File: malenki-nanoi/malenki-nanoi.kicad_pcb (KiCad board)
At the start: 4 copper layers, 19 x 32 mm, 45 parts, among them J1 Conn_01x02_Male-Connector, J2 Conn_01x08_Male, J3 Conn_01x02, J4 Conn_01x02_Male-Connector, J5 Conn_01x02_Male-Connector, J6 Conn_01x02_Male-Connector, U1 A7105, U2 AIC1734-33GUTR, U3 ATtiny1616-M, U4 DRV8837DSGR, U5 DRV8837DSGR, U6 DRV8837DSGR, Y1 16 Mhz 20ppm

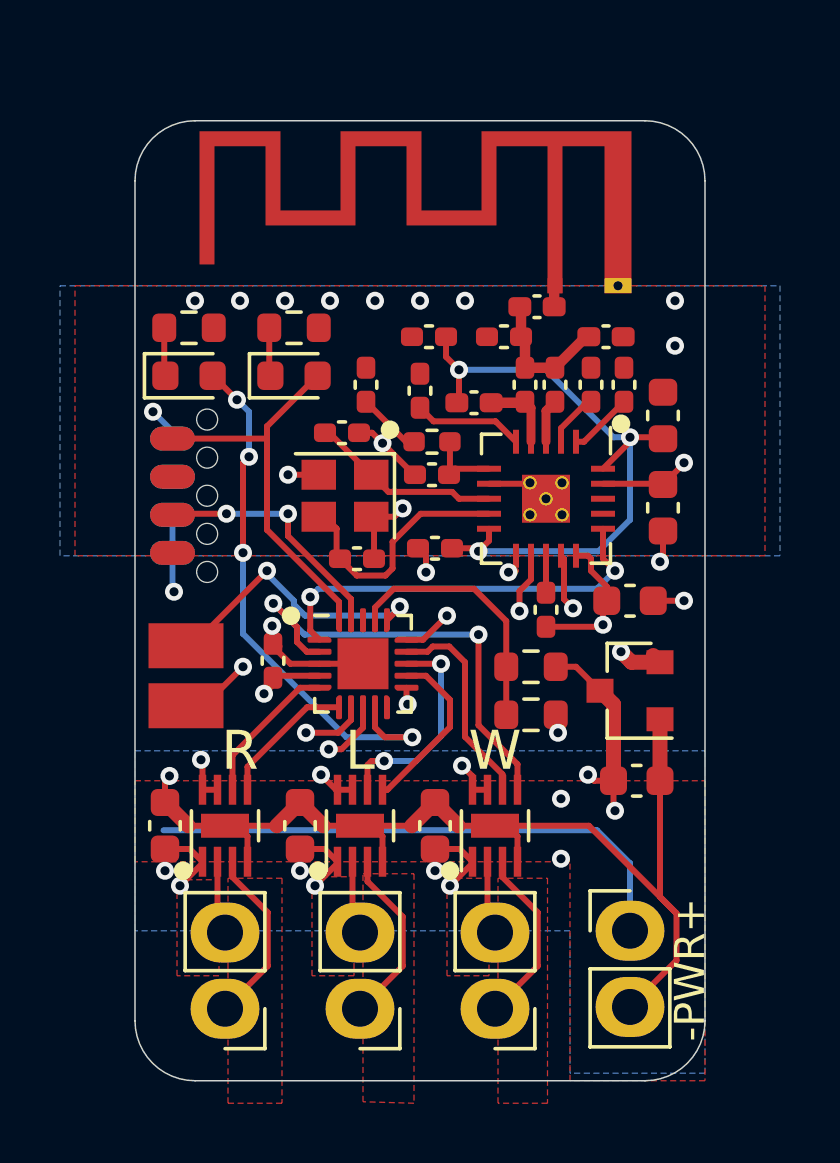
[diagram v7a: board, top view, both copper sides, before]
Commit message: Change crystal
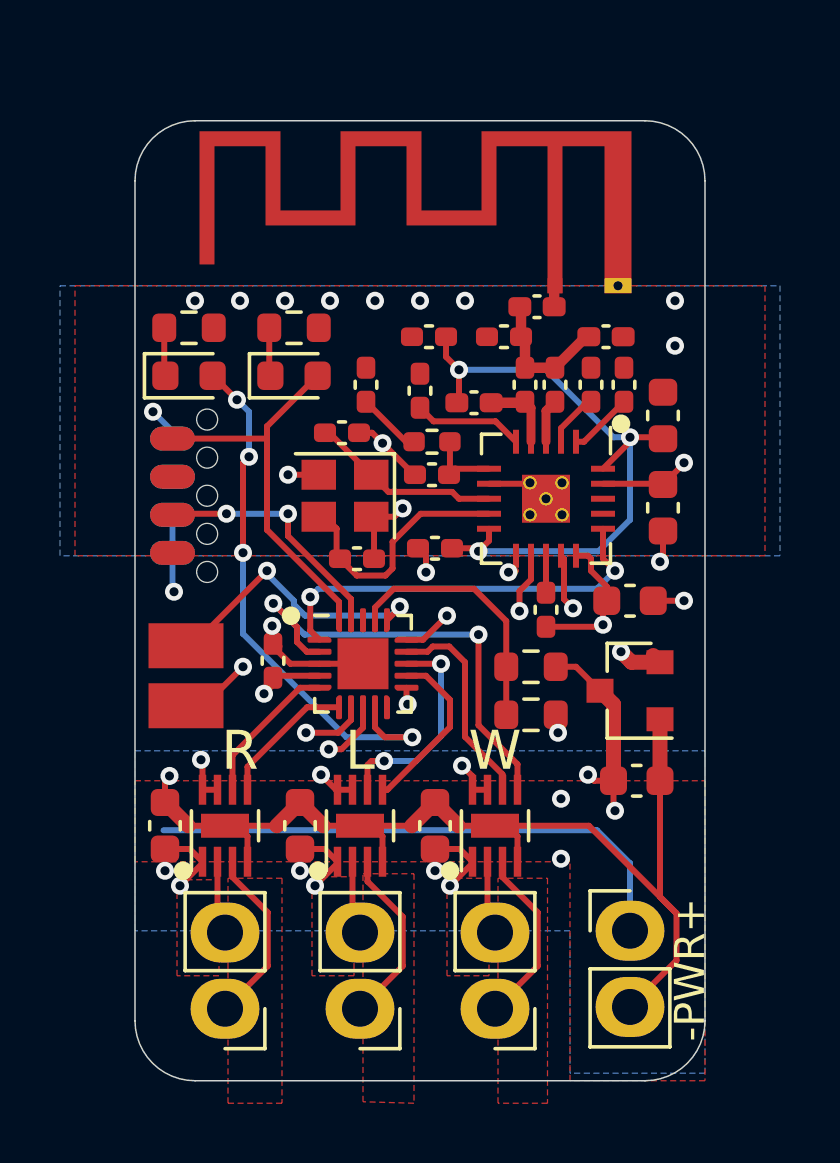
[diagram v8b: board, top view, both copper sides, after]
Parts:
- C14, C15: value 22pF -> 10pF
- Y1: value 16 Mhz 20ppm -> 16mhz Seiko Epson Q24FA20H0051200
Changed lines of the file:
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@@
     (thickness 1.6)
   )
-  (paper "A4")
+  (paper "A4" portrait)
   (title_block
     (title "Malenki-nano XS")
@@
       (effects (font (size 1 1) (thickness 0.15)))
     )
-    (fp_text value "22pF" (at 0 1.16) (layer "F.Fab")
+    (fp_text value "10pF" (at 0 1.16) (layer "F.Fab")
       (effects (font (size 1 1) (thickness 0.15)))
     )
@@
       (effects (font (size 1 1) (thickness 0.15)))
     )
-    (fp_text value "22pF" (at 0 1.16 180) (layer "F.Fab")
+    (fp_text value "10pF" (at 0 1.16 180) (layer "F.Fab")
       (effects (font (size 1 1) (thickness 0.15)))
     )
@@
     (property "Sheet file" "malenki-nanoi.kicad_sch")
     (property "Sheet name" "")
-    (attr through_hole)
+    (property "exclude_from_bom" "")
+    (attr through_hole exclude_from_bom)
     (fp_text reference "J1" (at 0 -2.33) (layer "F.SilkS") hide
       (effects (font (size 1 1) (thickness 0.15)))
@@
     (property "Sheet file" "motor_driver.kicad_sch")
     (property "Sheet name" "motor_driver_1_weapon")
-    (attr through_hole)
+    (property "exclude_from_bom" "")
+    (attr through_hole exclude_from_bom)
     (fp_text reference "J4" (at 0 -2.33) (layer "F.SilkS") hide
       (effects (font (size 1 1) (thickness 0.15)))
@@
     (property "Sheet file" "motor_driver.kicad_sch")
     (property "Sheet name" "motor_driver_3_right")
-    (attr through_hole)
+    (property "exclude_from_bom" "")
+    (attr through_hole exclude_from_bom)
     (fp_text reference "J6" (at 0 -2.33) (layer "F.SilkS") hide
       (effects (font (size 1 1) (thickness 0.15)))
@@
     (descr "SMD Crystal SERIES SMD2520/4 http://www.newxtal.com/UploadFiles/Images/2012-11-12-09-29-09-776.pdf, 2.5x2.0mm^2 package")
     (tags "SMD SMT crystal")
-    (property "LCSC" "C179632")
+    (property "LCSC" "C255947")
     (property "Sheet file" "radio.kicad_sch")
     (property "Sheet name" "radio")
@@
       (effects (font (size 1 1) (thickness 0.15)))
     )
-    (fp_text value "16 Mhz 20ppm" (at 0 2.2) (layer "F.Fab") hide
+    (fp_text value "16mhz Seiko Epson Q24FA20H0051200 " (at 0 2.2) (layer "F.Fab") hide
       (effects (font (size 1 1) (thickness 0.15)))
     )
@@
     (property "Sheet file" "motor_driver.kicad_sch")
     (property "Sheet name" "motor_driver_2_left")
-    (attr through_hole)
+    (property "exclude_from_bom" "")
+    (attr through_hole exclude_from_bom)
     (fp_text reference "J5" (at 0 -2.33) (layer "F.SilkS") hide
       (effects (font (size 1 1) (thickness 0.15)))
@@
     (property "Sheet file" "malenki-nanoi.kicad_sch")
     (property "Sheet name" "")
-    (attr through_hole)
+    (property "exclude_from_bom" "")
+    (attr through_hole exclude_from_bom)
     (fp_text reference "J2" (at 0 3.302 -90) (layer "B.SilkS") hide
       (effects (font (size 1 1) (thickness 0.15)) (justify mirror))
@@
   (gr_circle (center 98.5 74.5) (end 98.75 74.5) (layer "F.SilkS") (width 0.12) (fill solid))
   (gr_circle (center 93.2 66) (end 93.45 66) (layer "F.SilkS") (width 0.12) (fill solid))
-  (gr_circle (center 96.5 59.8) (end 96.75 59.8) (layer "F.SilkS") (width 0.12) (fill solid))
   (gr_circle (center 94.1 74.5) (end 94.35 74.5) (layer "F.SilkS") (width 0.12) (fill solid))
   (gr_circle (center 89.6 74.5) (end 89.85 74.5) (layer "F.SilkS") (width 0.12) (fill solid))
